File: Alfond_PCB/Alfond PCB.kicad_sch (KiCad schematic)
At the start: 39 parts, among them J3 Conn_01x05_Pin, J5 USB_B_Micro, P1 PHR-2, SW1 SW_SPDT, U1 DS18B20, U2 STM32U545VETx, U3 MIC5219-3.3YMM, U4 INA260, Y1 16MHz

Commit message: Add files via upload
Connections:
- no-connect marks 92 -> 90

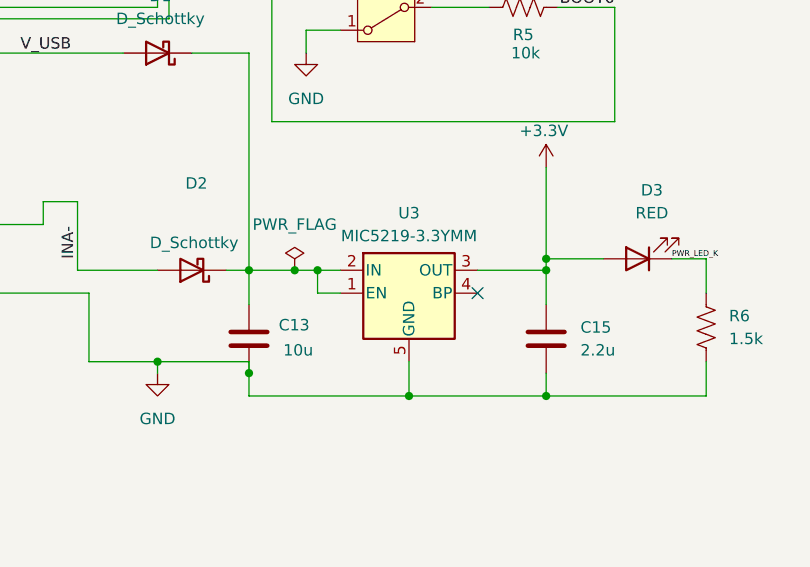
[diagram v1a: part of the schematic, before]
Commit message: Update to PCB and Footprints
The PCB was updated to the correct MIC ordered from Digikey, and the footprint was added to the footprint folders.
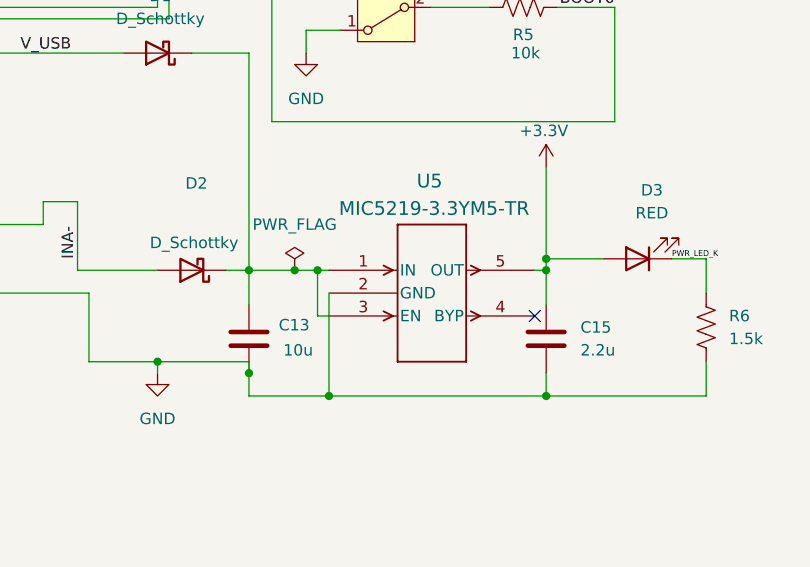
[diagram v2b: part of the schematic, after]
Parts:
- removed U3: MIC5219-3.3YMM, Package_SO:MSOP-8_3x3mm_P0.65mm, symbol Regulator_Linear:MIC5219-3.3YMM
- added U5: MIC5219-3.3YM5-TR, SOT-23-5_M5_MCH, symbol 2024-11-27_18-10-07:MIC5219-3.3YM5-TR
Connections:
- net +3.3V: now also U5.5 (OUT)
- net GND: now also U5.2 (GND)
- net at C13.1, D1.1 (K), D2.1 (K): now also U5.1 (IN), U5.3 (EN)
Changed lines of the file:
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@@
 	)
 	(junction
+		(at 232.41 160.02)
+		(diameter 0)
+		(color 0 0 0 0)
+	)
+	(junction
 		(at 125.73 40.64)
 		(diameter 0)
@@
 	)
 	(junction
+		(at 256.54 146.05)
+		(diameter 0)
+		(color 0 0 0 0)
+	)
+	(junction
 		(at 256.54 160.02)
 		(diameter 0)
@@
 	)
 	(junction
-		(at 256.54 146.05)
+		(at 231.14 146.05)
 		(diameter 0)
 		(color 0 0 0 0)
@@
 	)
 	(junction
-		(at 241.3 160.02)
-		(diameter 0)
-		(color 0 0 0 0)
-	)
-	(junction
 		(at 82.55 41.91)
 		(diameter 0)
@@
 	)
 	(junction
-		(at 231.14 146.05)
-		(diameter 0)
-		(color 0 0 0 0)
-	)
-	(junction
 		(at 130.81 40.64)
 		(diameter 0)
@@
 	)
 	(no_connect
+		(at 255.27 151.13)
+	)
+	(no_connect
 		(at 156.21 161.29)
 	)
@@
 	)
 	(no_connect
-		(at 248.92 148.59)
-	)
-	(no_connect
 		(at 232.41 83.82)
 	)
@@
 	(wire
 		(pts
-			(xy 233.68 148.59) (xy 231.14 148.59)
+			(xy 256.54 146.05) (xy 256.54 149.86)
+		)
+		(stroke
+			(width 0)
+			(type default)
+		)
+	)
+	(wire
+		(pts
+			(xy 232.41 160.02) (xy 256.54 160.02)
 		)
 		(stroke
@@
 	(wire
 		(pts
+			(xy 255.27 146.05) (xy 256.54 146.05)
+		)
+		(stroke
+			(width 0)
+			(type default)
+		)
+	)
+	(wire
+		(pts
 			(xy 96.52 163.83) (xy 96.52 175.26)
 		)
@@
 	(wire
 		(pts
-			(xy 231.14 148.59) (xy 231.14 146.05)
+			(xy 231.14 146.05) (xy 231.14 151.13)
 		)
 		(stroke
@@
 	(wire
 		(pts
-			(xy 104.14 41.91) (xy 113.03 41.91)
+			(xy 231.14 146.05) (xy 232.41 146.05)
 		)
 		(stroke
@@
 	(wire
 		(pts
-			(xy 99.06 110.49) (xy 99.06 115.57)
+			(xy 104.14 41.91) (xy 113.03 41.91)
 		)
 		(stroke
@@
 	(wire
 		(pts
-			(xy 133.35 40.64) (xy 130.81 40.64)
+			(xy 99.06 110.49) (xy 99.06 115.57)
 		)
 		(stroke
@@
 	(wire
 		(pts
-			(xy 93.98 62.23) (xy 93.98 59.69)
+			(xy 133.35 40.64) (xy 130.81 40.64)
 		)
 		(stroke
@@
 	(wire
 		(pts
-			(xy 264.16 129.54) (xy 226.06 129.54)
+			(xy 93.98 62.23) (xy 93.98 59.69)
 		)
 		(stroke
@@
 	(wire
 		(pts
-			(xy 200.66 140.97) (xy 200.66 138.43)
+			(xy 264.16 129.54) (xy 226.06 129.54)
 		)
 		(stroke
@@
 	(wire
 		(pts
-			(xy 165.1 124.46) (xy 173.99 124.46)
+			(xy 200.66 140.97) (xy 200.66 138.43)
 		)
 		(stroke
@@
 	(wire
 		(pts
-			(xy 241.3 156.21) (xy 241.3 160.02)
+			(xy 165.1 124.46) (xy 173.99 124.46)
 		)
 		(stroke
@@
 	(wire
 		(pts
-			(xy 231.14 146.05) (xy 233.68 146.05)
+			(xy 36.83 106.68) (xy 36.83 110.49)
 		)
 		(stroke
@@
 	(wire
 		(pts
-			(xy 36.83 106.68) (xy 36.83 110.49)
+			(xy 232.41 148.59) (xy 232.41 160.02)
 		)
 		(stroke
@@
 	(wire
 		(pts
-			(xy 223.52 160.02) (xy 241.3 160.02)
+			(xy 223.52 160.02) (xy 232.41 160.02)
 		)
 		(stroke
@@
 	(wire
 		(pts
-			(xy 248.92 146.05) (xy 256.54 146.05)
-		)
-		(stroke
-			(width 0)
-			(type default)
-		)
-	)
-	(wire
-		(pts
 			(xy 19.05 140.97) (xy 19.05 144.78)
 		)
@@
 	(wire
 		(pts
-			(xy 256.54 146.05) (xy 256.54 149.86)
-		)
-		(stroke
-			(width 0)
-			(type default)
-		)
-	)
-	(wire
-		(pts
 			(xy 25.4 77.47) (xy 25.4 80.01)
 		)
@@
 	(wire
 		(pts
-			(xy 241.3 160.02) (xy 256.54 160.02)
+			(xy 257.81 116.84) (xy 264.16 116.84)
 		)
 		(stroke
@@
 	(wire
 		(pts
-			(xy 257.81 116.84) (xy 264.16 116.84)
+			(xy 22.86 64.77) (xy 25.4 64.77)
 		)
 		(stroke
@@
 	(wire
 		(pts
-			(xy 22.86 64.77) (xy 25.4 64.77)
+			(xy 71.12 34.29) (xy 82.55 34.29)
 		)
 		(stroke
@@
 	(wire
 		(pts
-			(xy 71.12 34.29) (xy 82.55 34.29)
+			(xy 256.54 157.48) (xy 256.54 160.02)
 		)
 		(stroke
@@
 	(wire
 		(pts
-			(xy 256.54 157.48) (xy 256.54 160.02)
+			(xy 187.96 139.7) (xy 187.96 140.97)
 		)
 		(stroke
@@
 	(wire
 		(pts
-			(xy 187.96 139.7) (xy 187.96 140.97)
+			(xy 231.14 151.13) (xy 232.41 151.13)
 		)
 		(stroke
@@
 	)
 	(symbol
+		(lib_id "2024-11-27_18-10-07:MIC5219-3.3YM5-TR")
+		(at 232.41 146.05 0)
+		(unit 1)
+		(exclude_from_sim no)
+		(in_bom yes)
+		(on_board yes)
+		(dnp no)
+		(property "Reference" "U5"
+			(at 243.586 136.144 0)
+			(effects
+				(font
+					(size 1.524 1.524)
+				)
+			)
+		)
+		(property "Value" "MIC5219-3.3YM5-TR"
+			(at 244.094 139.192 0)
+			(effects
+				(font
+					(size 1.524 1.524)
+				)
+			)
+		)
+		(property "Footprint" "SOT-23-5_M5_MCH"
+			(at 232.41 146.05 0)
+			(effects
+				(font
+					(size 1.27 1.27)
+					(italic yes)
+				)
+				(hide yes)
+			)
+		)
+		(property "Datasheet" "MIC5219-3.3YM5-TR"
+			(at 232.41 146.05 0)
+			(effects
+				(font
+					(size 1.27 1.27)
+					(italic yes)
+				)
+				(hide yes)
+			)
+		)
+		(property "Description" ""
+			(at 232.41 146.05 0)
+			(effects
+				(font
+					(size 1.27 1.27)
+				)
+				(hide yes)
+			)
+		)
+		(pin "4"
+		)
+		(pin "1"
+		)
+		(pin "3"
+		)
+		(pin "5"
+		)
+		(pin "2"
+		)
+		(instances
+			(project ""
+				(path "/a49d69de-c8cc-4590-9df8-ae7f598e37d2"
+					(reference "U5")
+					(unit 1)
+				)
+			)
+		)
+	)
+	(symbol
 		(lib_id "PHR-2:PHR-2")
 		(at 177.8 147.32 180)
@@
 		(on_board yes)
 		(dnp no)
-		(fields_autoplaced yes)
 		(property "Reference" "R6"
 			(at 276.86 151.1299 0)
@@
 					(unit 1)
 				)
-			)
-		)
-	)
-	(symbol
-		(lib_id "Regulator_Linear:MIC5219-3.3YMM")
-		(at 241.3 148.59 0)
-		(unit 1)
-		(exclude_from_sim no)
-		(in_bom yes)
-		(on_board yes)
-		(dnp no)
-		(fields_autoplaced yes)
-		(property "Reference" "U3"
-			(at 241.3 139.7 0)
-			(effects
-				(font
-					(size 1.27 1.27)
-				)
-			)
-		)
-		(property "Value" "MIC5219-3.3YMM"
-			(at 241.3 142.24 0)
-			(effects
-				(font
-					(size 1.27 1.27)
-				)
-			)
-		)
-		(property "Footprint" "Package_SO:MSOP-8_3x3mm_P0.65mm"
-			(at 241.3 140.335 0)
-			(effects
-				(font
-					(size 1.27 1.27)
-				)
-				(hide yes)
-			)
-		)
-		(property "Datasheet" "http://ww1.microchip.com/downloads/en/DeviceDoc/MIC5219-500mA-Peak-Output-LDO-Regulator-DS20006021A.pdf"
-			(at 241.3 148.59 0)
-			(effects
-				(font
-					(size 1.27 1.27)
-				)
-				(hide yes)
-			)
-		)
-		(property "Description" "500mA low dropout linear regulator, fixed 3.3V output, MSOP-8"
-			(at 241.3 148.59 0)
-			(effects
-				(font
-					(size 1.27 1.27)
-				)
-				(hide yes)
-			)
-		)
-		(pin "3"
-		)
-		(pin "5"
-		)
-		(pin "6"
-		)
-		(pin "2"
-		)
-		(pin "8"
-		)
-		(pin "7"
-		)
-		(pin "4"
-		)
-		(pin "1"
-		)
-		(instances
-			(project ""
-				(path "/a49d69de-c8cc-4590-9df8-ae7f598e37d2"
-					(reference "U3")
-					(unit 1)
-				)

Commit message: fixed few errors
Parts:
- removed U5: MIC5219-3.3YM5-TR, SOT-23-5_M5_MCH, symbol 2024-11-27_18-10-07:MIC5219-3.3YM5-TR
- added U3: MIC5219-3.3YMM, Package_SO:MSOP-8_3x3mm_P0.65mm, symbol Regulator_Linear:MIC5219-3.3YMM
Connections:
- net +3.3V: now also U3.3 (OUT)
- net GND: now also U3.5 (GND), U3.6 (GND), U3.7 (GND), U3.8 (GND)
- net at C13.1, D1.1 (K), D2.1 (K): now also U3.1 (EN), U3.2 (IN)
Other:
- moved on the sheet: P1

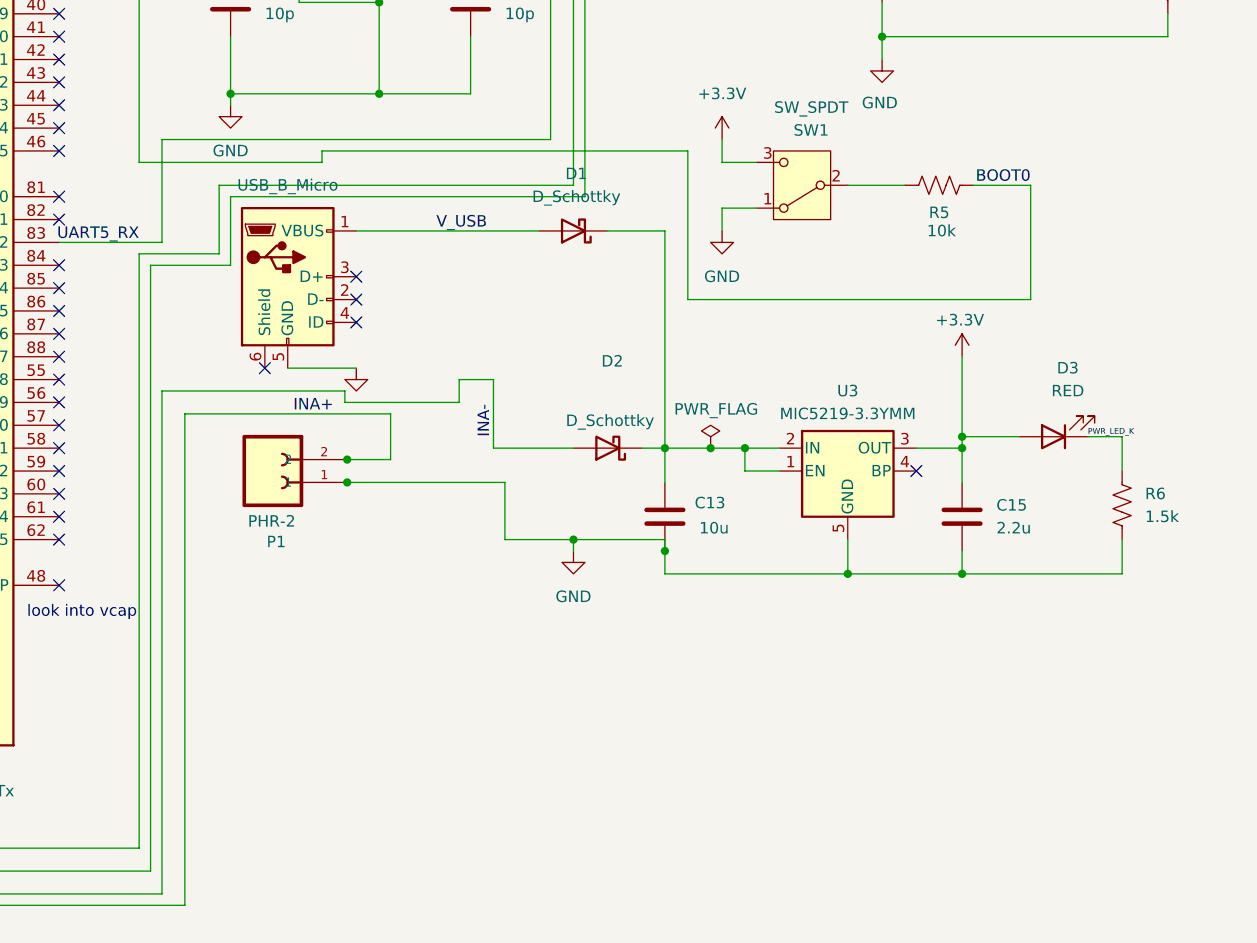
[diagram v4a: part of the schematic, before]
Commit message: Final PCB Changes
Changed the Schottky diodes to the MAX40200 diodes
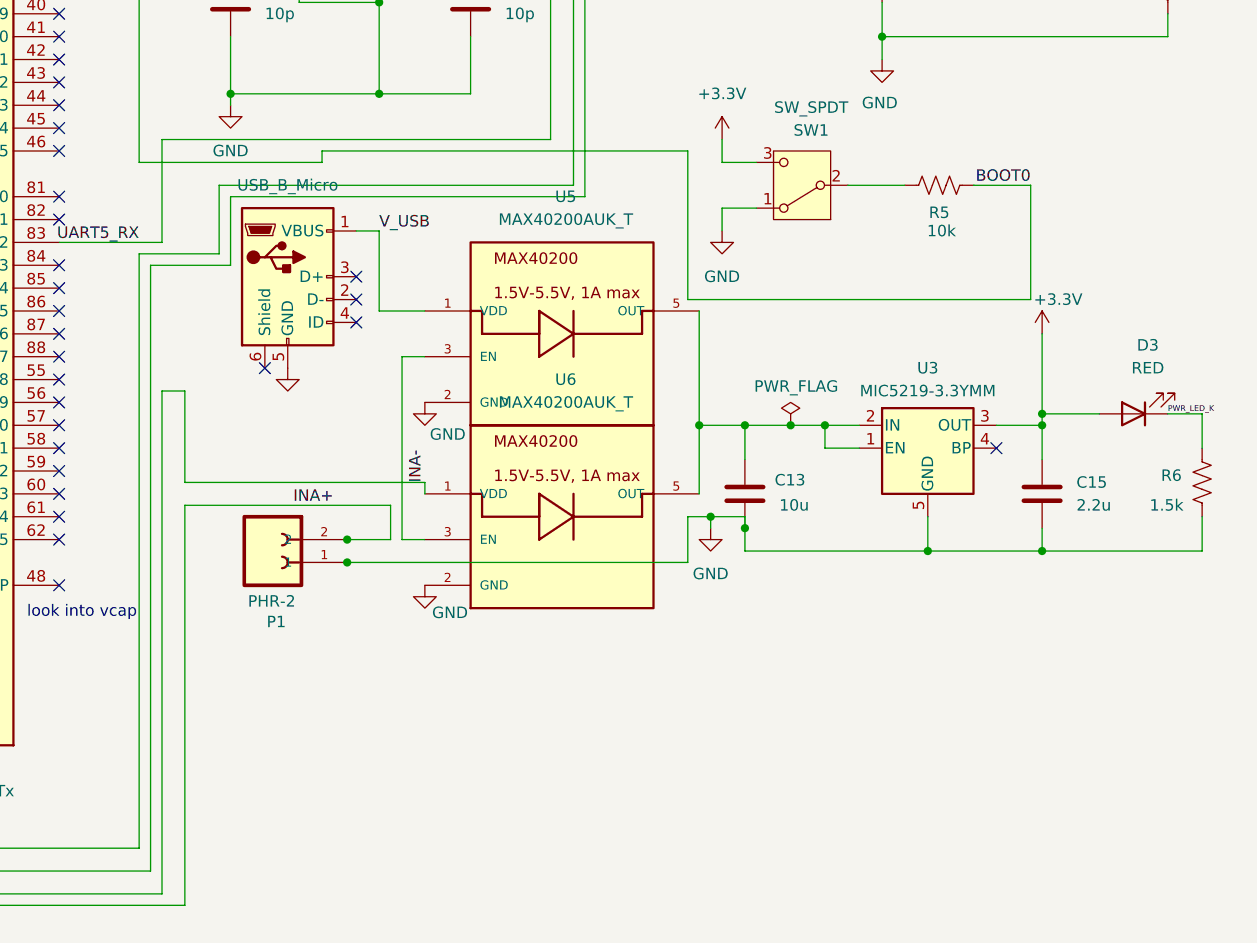
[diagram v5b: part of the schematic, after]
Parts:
- removed D1, D2: D_Schottky, Diode_SMD:D_SOD-123, symbol Device:D_Schottky
- added U5, U6: MAX40200AUK_T, MAX40200AUK_T:SOT-23-5, symbol MAX40200AUK_T:MAX40200AUK_T
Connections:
- net GND: now also U5.2 (GND), U6.2 (GND)
- net INA-: now also U6.1 (VDD)
- net V_USB: now also U5.1 (VDD)
- net at C13.1, U3.1 (EN), U3.2 (IN): now also U5.5 (OUT), U6.5 (OUT)
- new net: U5.3 (EN), U6.3 (EN)
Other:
- moved on the sheet: C13, C15, D3, P1, R6, U3

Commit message: made improvments to pcb
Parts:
- added H1, H2, H3, H4: MountingHole, MountingHole:MountingHole_2.2mm_M2, symbol Mechanical:MountingHole
- C1: footprint Capacitor_SMD:C_0603_1608Metric -> Capacitor_SMD:C_0805_2012Metric_Pad1.18x1.45mm_HandSolder
- C10, C11, C12, C2, C3, C4, C5, C6, C7, C8, C9: footprint Capacitor_SMD:C_0402_1005Metric_Pad0.74x0.62mm_HandSolder -> Capacitor_SMD:C_0805_2012Metric_Pad1.18x1.45mm_HandSolder
- C14: footprint Capacitor_SMD:C_01005_0402Metric_Pad0.57x0.30mm_HandSolder -> Capacitor_SMD:C_0805_2012Metric_Pad1.18x1.45mm_HandSolder
- J5: footprint Connector_USB:USB_Micro-B_Wuerth_629105150521 -> Connector_USB:USB_Micro-B_Amphenol_10118193-0001LF_Horizontal
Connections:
- net I2C1_SCL: now also U2.95 (PB8); no longer U2.96 (PB9)
- net I2C1_SDA: now also U2.96 (PB9); no longer U2.95 (PB8)
- net I2C2_SCL: now also U2.47 (PB10); no longer U2.53 (PB14)
- net I2C2_SDA: now also U2.53 (PB14); no longer U2.47 (PB10)
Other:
- note added: "Mounting Holes"
- note removed: "add a button for the boot0 pin"
- note removed: "add a reset button for the ucontroller"
- note removed: "add a swd programming header on for programming"

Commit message: made changes to switch placement
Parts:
- R1, R3, R4, R5, R6, R7: footprint Resistor_SMD:R_0402_1005Metric_Pad0.72x0.64mm_HandSolder -> Resistor_SMD:R_0603_1608Metric_Pad0.98x0.95mm_HandSolder
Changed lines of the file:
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@@
 			)
 		)
-		(property "Footprint" "Resistor_SMD:R_0402_1005Metric_Pad0.72x0.64mm_HandSolder"
+		(property "Footprint" "Resistor_SMD:R_0603_1608Metric_Pad0.98x0.95mm_HandSolder"
 			(at 280.416 94.234 90)
 			(effects
@@
 			)
 		)
-		(property "Footprint" "Resistor_SMD:R_0402_1005Metric_Pad0.72x0.64mm_HandSolder"
+		(property "Footprint" "Resistor_SMD:R_0603_1608Metric_Pad0.98x0.95mm_HandSolder"
 			(at 41.656 56.134 90)
 			(effects
@@
 			)
 		)
-		(property "Footprint" "Resistor_SMD:R_0402_1005Metric_Pad0.72x0.64mm_HandSolder"
+		(property "Footprint" "Resistor_SMD:R_0603_1608Metric_Pad0.98x0.95mm_HandSolder"
 			(at 50.546 112.014 90)
 			(effects
@@
 			)
 		)
-		(property "Footprint" "Resistor_SMD:R_0402_1005Metric_Pad0.72x0.64mm_HandSolder"
+		(property "Footprint" "Resistor_SMD:R_0603_1608Metric_Pad0.98x0.95mm_HandSolder"
 			(at 33.274 61.214 90)
 			(effects
@@
 			)
 		)
-		(property "Footprint" "Resistor_SMD:R_0402_1005Metric_Pad0.72x0.64mm_HandSolder"
+		(property "Footprint" "Resistor_SMD:R_0603_1608Metric_Pad0.98x0.95mm_HandSolder"
 			(at 284.226 150.114 90)
 			(effects
@@
 			)
 		)
-		(property "Footprint" "Resistor_SMD:R_0402_1005Metric_Pad0.72x0.64mm_HandSolder"
+		(property "Footprint" "Resistor_SMD:R_0603_1608Metric_Pad0.98x0.95mm_HandSolder"
 			(at 254.254 115.824 90)
 			(effects
